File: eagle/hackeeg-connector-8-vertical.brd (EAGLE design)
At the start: 114.6 x 27.9 mm, 21 parts

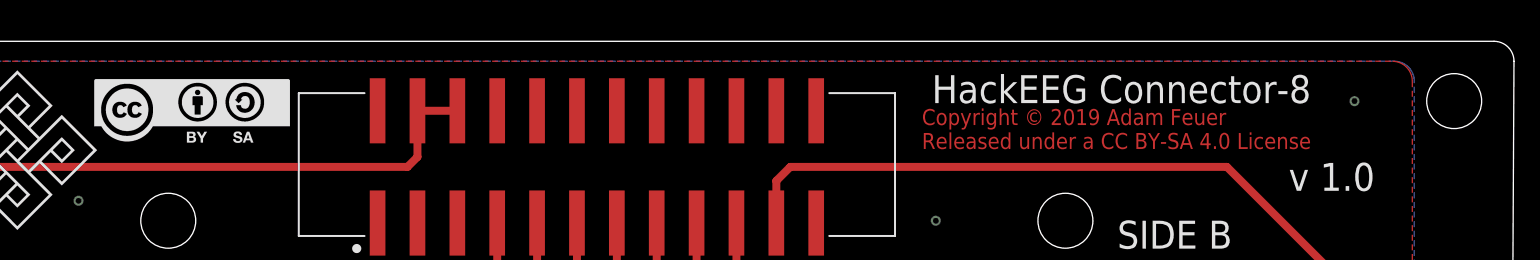
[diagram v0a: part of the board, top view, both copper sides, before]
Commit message: relicense to CERN OHL 1.2 - sch and brd
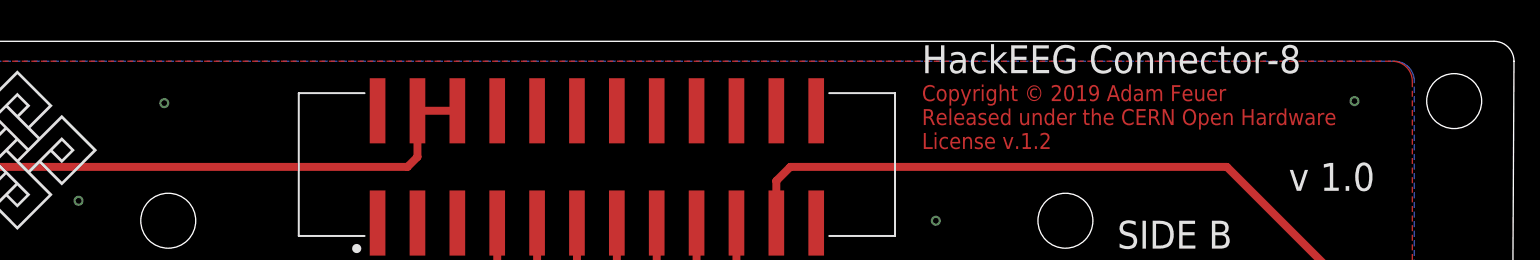
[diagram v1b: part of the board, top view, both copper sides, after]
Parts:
- removed FRAME1: FRAME-LETTER, SparkFun-Aesthetics:CREATIVE_COMMONS
- removed U$13: CC-BY-SA, creative-commons:CC-BY-SA
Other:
- board text added: "Copyright © 2019 Adam Feuer Released under the CERN Open Hardware License v.1.2"
- board text removed: "Copyright © 2019 Adam Feuer Released under a CC BY-SA 4.0 License"
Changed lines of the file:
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@@
 <board>
 <plain>
-<text x="76.581" y="23.622" size="1.016" layer="1">Copyright © 2019 Adam Feuer
-Released under a CC BY-SA 4.0 License</text>
+<text x="76.581" y="23.622" size="1.016" layer="1" font="vector" ratio="13">Copyright © 2019 Adam Feuer
+Released under the CERN Open Hardware
+License v.1.2</text>
 <hole x="3.81" y="26.67" drill="3.49999375"/>
 <hole x="3.81" y="6.35" drill="3.49999375"/>
@@
 <dimension x1="-2.54" y1="30.48" x2="-2.54" y2="2.54" x3="-8.89" y3="16.51" textsize="1.778" layer="47" unit="inch"/>
 <text x="99.949" y="20.955" size="1.778" layer="25">v 1.0</text>
-<text x="77.216" y="26.543" size="1.778" layer="25">HackEEG Connector-8</text>
+<text x="76.581" y="28.448" size="1.778" layer="25" font="vector">HackEEG Connector-8</text>
 </plain>
 <attributes>
@@
 <attribute name="VALUE" x="36.7749" y="14.83696875" size="1.78313125" layer="27"/>
 </element>
-<element name="FRAME1" library="SparkFun-Aesthetics" library_urn="urn:adsk.eagle:library:507" package="CREATIVE_COMMONS" package3d_urn="urn:adsk.eagle:package:37121/1" value="FRAME-LETTER" x="21.59" y="-10.16" smashed="yes"/>
 <element name="IN1P" library="po-37729" package="HEX-110" value="PO37729HEX-110" x="22.86" y="10.16" smashed="yes" rot="MR0">
 <attribute name="NAME" x="26.07" y="14.83" size="1.27" layer="26" rot="MR0"/>
@@
 </element>
 <element name="U$1" library="endless-knot" package="ENDLESSKNOT-MEDIUM" value="ENDLESSKNOTENDLESSKNOT-MEDIUM" x="17.653" y="23.495" smashed="yes"/>
-<element name="U$13" library="creative-commons" package="CC-BY-SA" value="CC-BY-SA" x="23.749" y="23.749" smashed="yes"/>
 <element name="IN8P" library="po-37729" package="HEX-110" value="PO37729HEX-110" x="102.87" y="10.16" smashed="yes" rot="MR0">
 <attribute name="NAME" x="106.08" y="14.83" size="1.27" layer="26" rot="MR0"/>

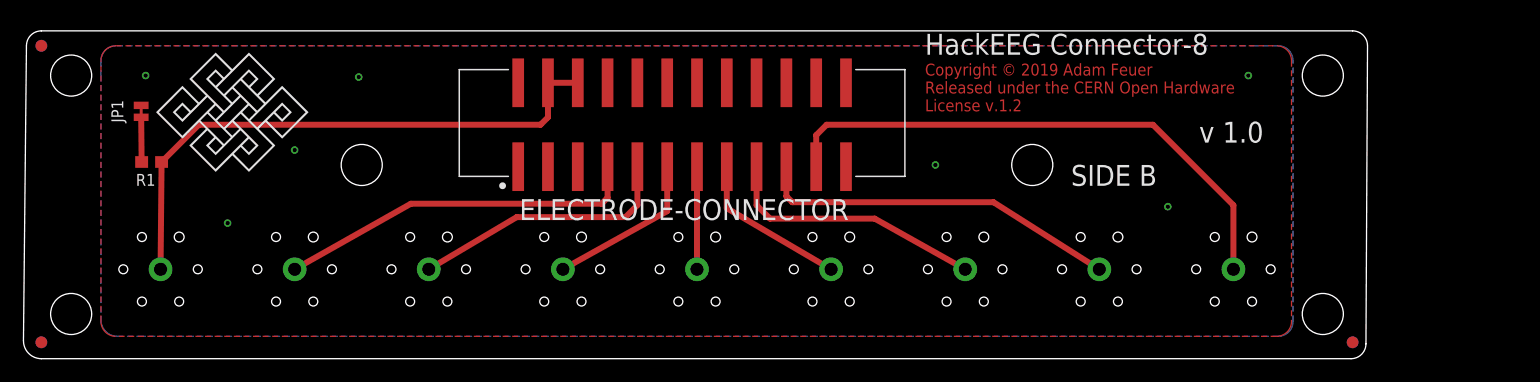
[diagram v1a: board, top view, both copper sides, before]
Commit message: add 2-pin JST connector for REF_ELEC multiboard
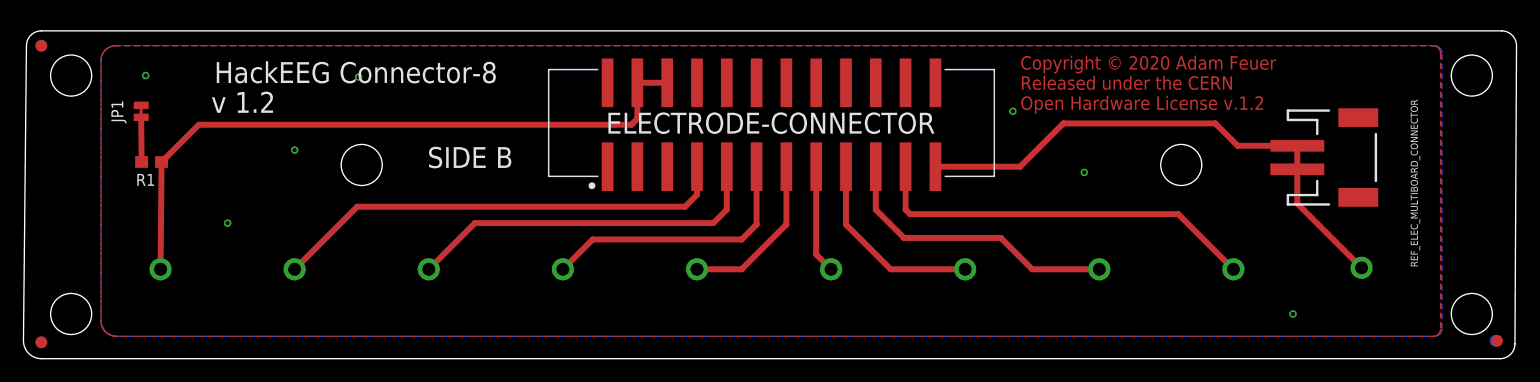
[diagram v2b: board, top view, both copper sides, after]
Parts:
- removed U$1: ENDLESSKNOTENDLESSKNOT-MEDIUM, endless-knot:ENDLESSKNOT-MEDIUM
- added REF_ELEC: PO37729_NO_STANDOFF_HOLES, hackeeg-connectors:SIMPLE0
- added REF_ELEC_MULTIBOARD_CONNECTOR: (no value), SparkFun-Connectors:JST-2-SMD
- AGND, IN1P, IN2P, IN3P, IN4P, IN5P, IN6P, IN7P, IN8P: value PO37729HEX-110 -> PO37729_NO_STANDOFF_HOLES; device po-37729:HEX-110 -> hackeeg-connectors:SIMPLE0
- moved FD3 12.3 mm to (125.3, 4.06)
- moved FD4 12.2 mm to (125.2, 4.06)
- moved ELECTRODE-CONNECTOR 7.62 mm to (63.5, 22.5)
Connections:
- new net REF_ELEC: ELECTRODE-CONNECTOR.23, REF_ELEC.P$1, REF_ELEC_MULTIBOARD_CONNECTOR.1, REF_ELEC_MULTIBOARD_CONNECTOR.2
- net AGND1: now also AGND.P$1; no longer AGND.SIGNAL
- net N$2: now also IN1P.P$1; no longer IN1P.SIGNAL
- net N$3: now also IN2P.P$1; no longer IN2P.SIGNAL
- net N$4: now also IN3P.P$1; no longer IN3P.SIGNAL
- net N$5: now also IN4P.P$1; no longer IN4P.SIGNAL
- net N$6: now also IN5P.P$1; no longer IN5P.SIGNAL
- net N$7: now also IN6P.P$1; no longer IN6P.SIGNAL
- net N$8: now also IN7P.P$1; no longer IN7P.SIGNAL
- net N$9: now also IN8P.P$1; no longer IN8P.SIGNAL
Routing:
- net REF_ELEC: track 0.00 -> 45.8 mm
- net N$9: track 46.9 -> 32.6 mm
- net N$3: track 22.7 -> 31.2 mm
- net N$4: track 14.0 -> 21.9 mm
- net N$8: track 31.1 -> 23.7 mm
- net N$2: track 31.0 -> 38.2 mm
- net N$7: track 22.7 -> 16.7 mm
- net AGND1: track 49.1 -> 54.9 mm
- net N$6: track 13.8 -> 8.15 mm
- net N$5: track 8.74 -> 13.0 mm
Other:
- board size 114.6 x 27.9 mm -> 127.3 x 27.9 mm
- board text added: "Copyright © 2020 Adam Feuer Released under the CERN Open Hardware License v.1.2"
- board text added: "v 1.2"
- board text removed: "Copyright © 2019 Adam Feuer Released under the CERN Open Hardware License v.1.2"
- board text removed: "v 1.0"
